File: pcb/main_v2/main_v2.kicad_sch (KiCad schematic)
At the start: 1 part, among them J101 Conn_02x08_Top_Bottom

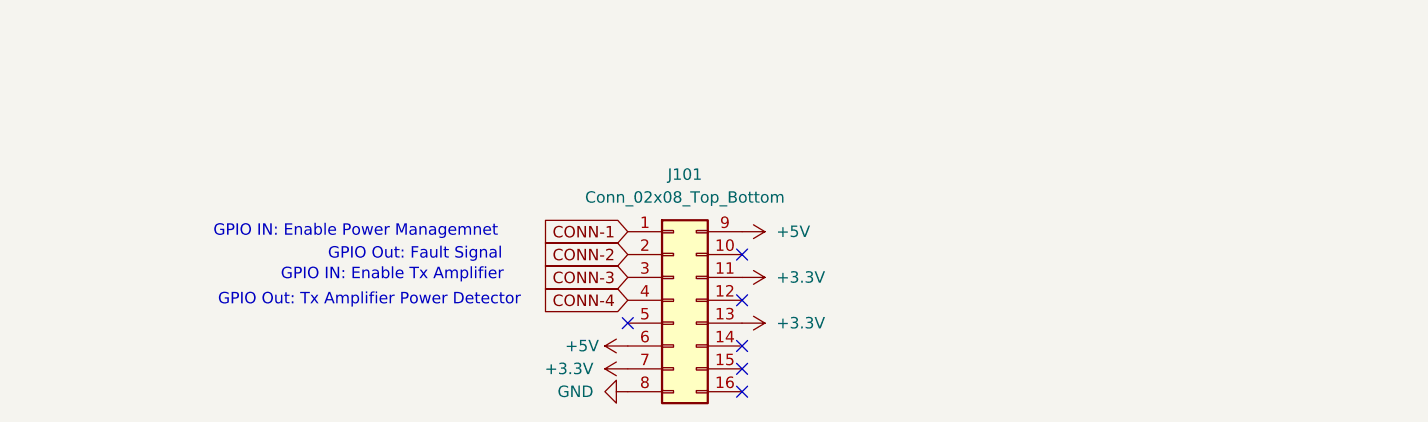
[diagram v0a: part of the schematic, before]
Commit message: updated layout
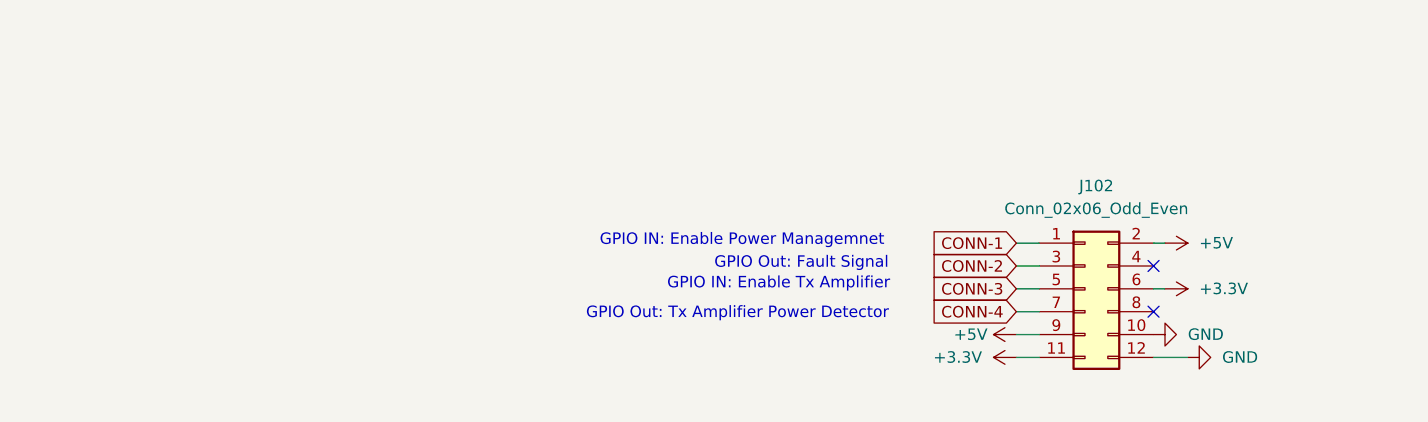
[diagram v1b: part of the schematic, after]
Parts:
- removed J101: Conn_02x08_Top_Bottom, Connector_PinHeader_2.54mm:PinHeader_2x08_P2.54mm_Vertical_SMD, symbol Connector_Generic:Conn_02x08_Top_Bottom
- added J102: Conn_02x06_Odd_Even, symbol Connector_Generic:Conn_02x06_Odd_Even
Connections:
- net +3.3V: now also J102.11 (Pin_11), J102.6 (Pin_6)
- net +5V: now also J102.2 (Pin_2), J102.9 (Pin_9)
- net CONN-1: now also J102.1 (Pin_1)
- net CONN-2: now also J102.3 (Pin_3)
- net CONN-3: now also J102.5 (Pin_5)
- net CONN-4: now also J102.7 (Pin_7)
- net GND: now also J102.10 (Pin_10), J102.12 (Pin_12)
- no-connect marks 6 -> 2
